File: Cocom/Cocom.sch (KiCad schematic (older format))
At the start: 19 parts

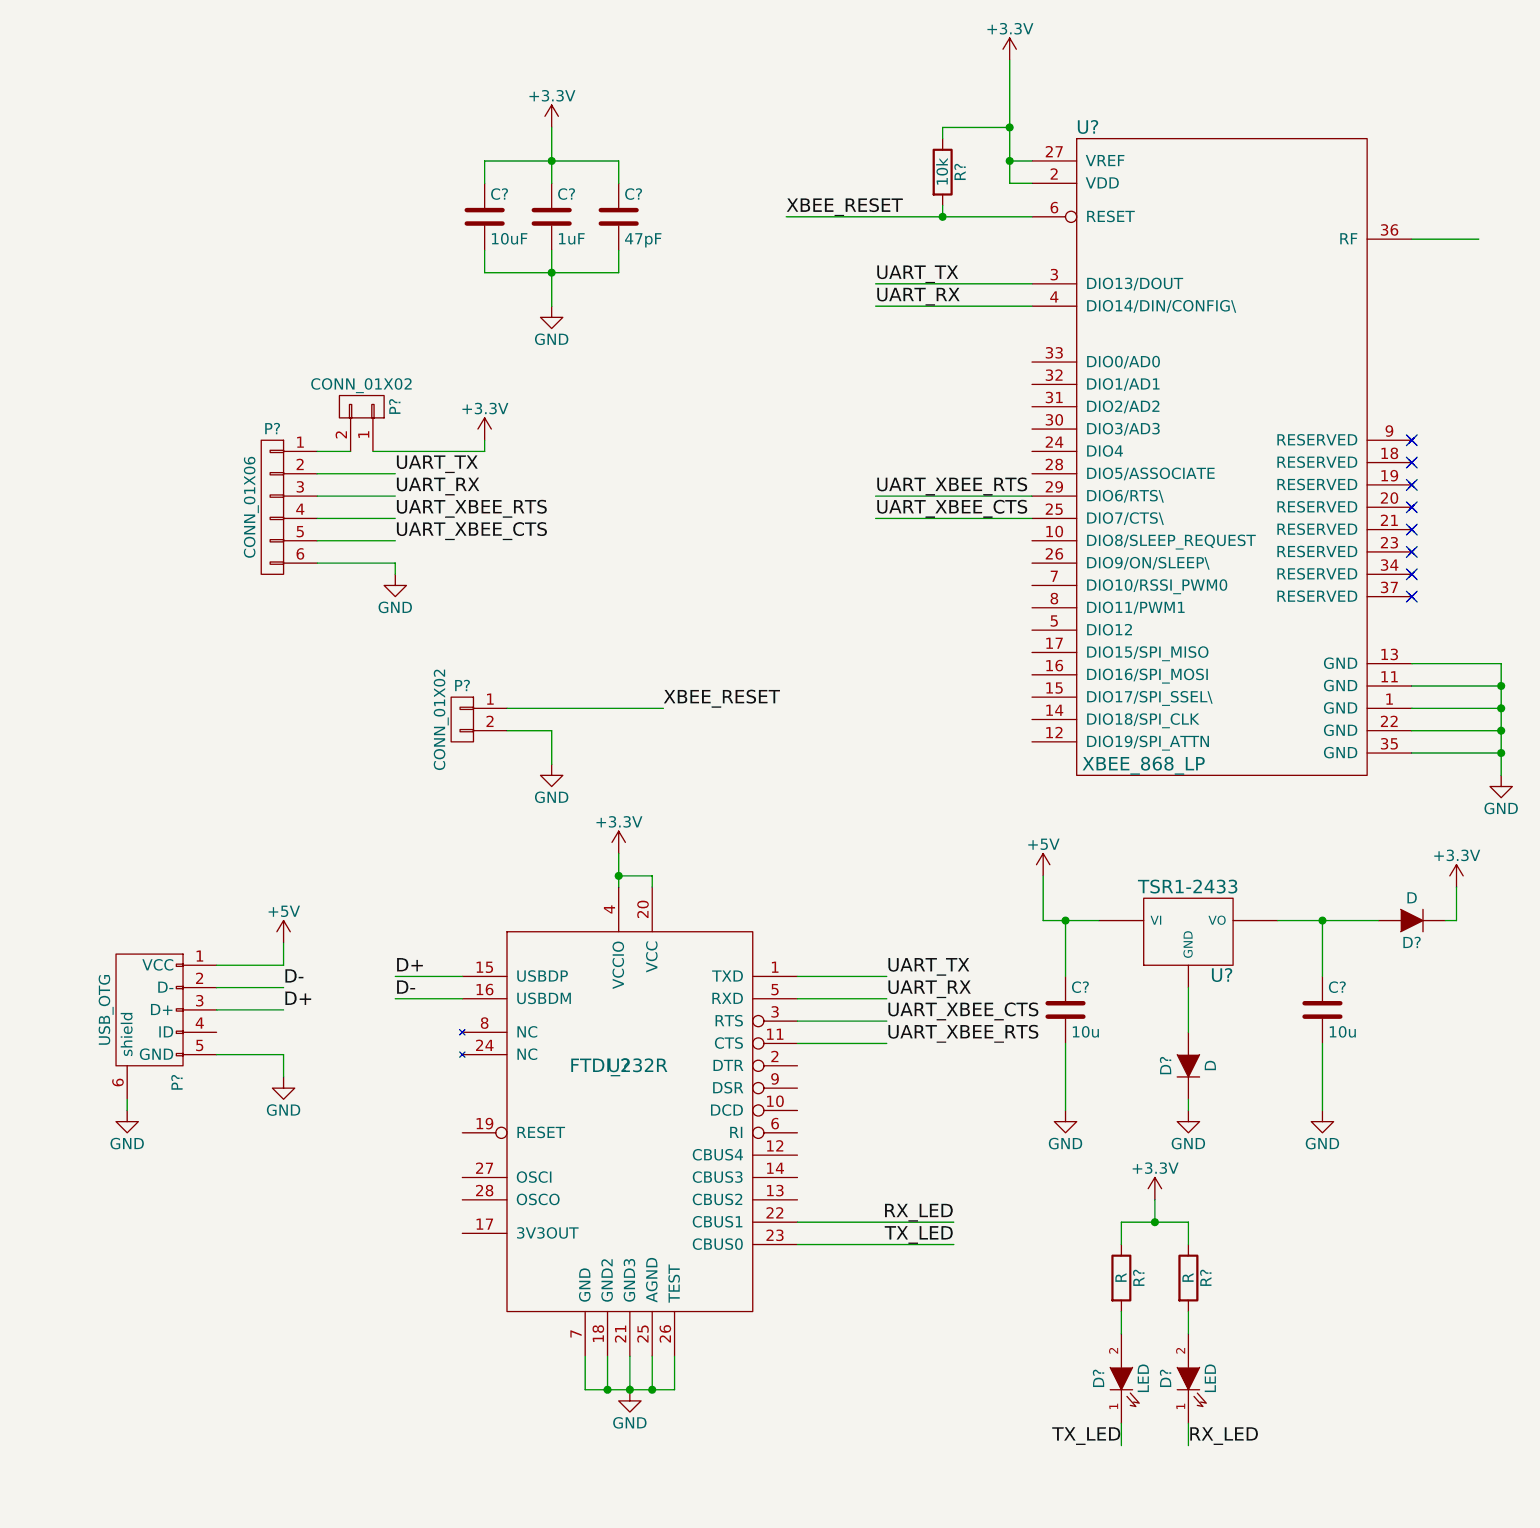
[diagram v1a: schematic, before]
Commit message: Add Cocom sch + pcb + some footprint
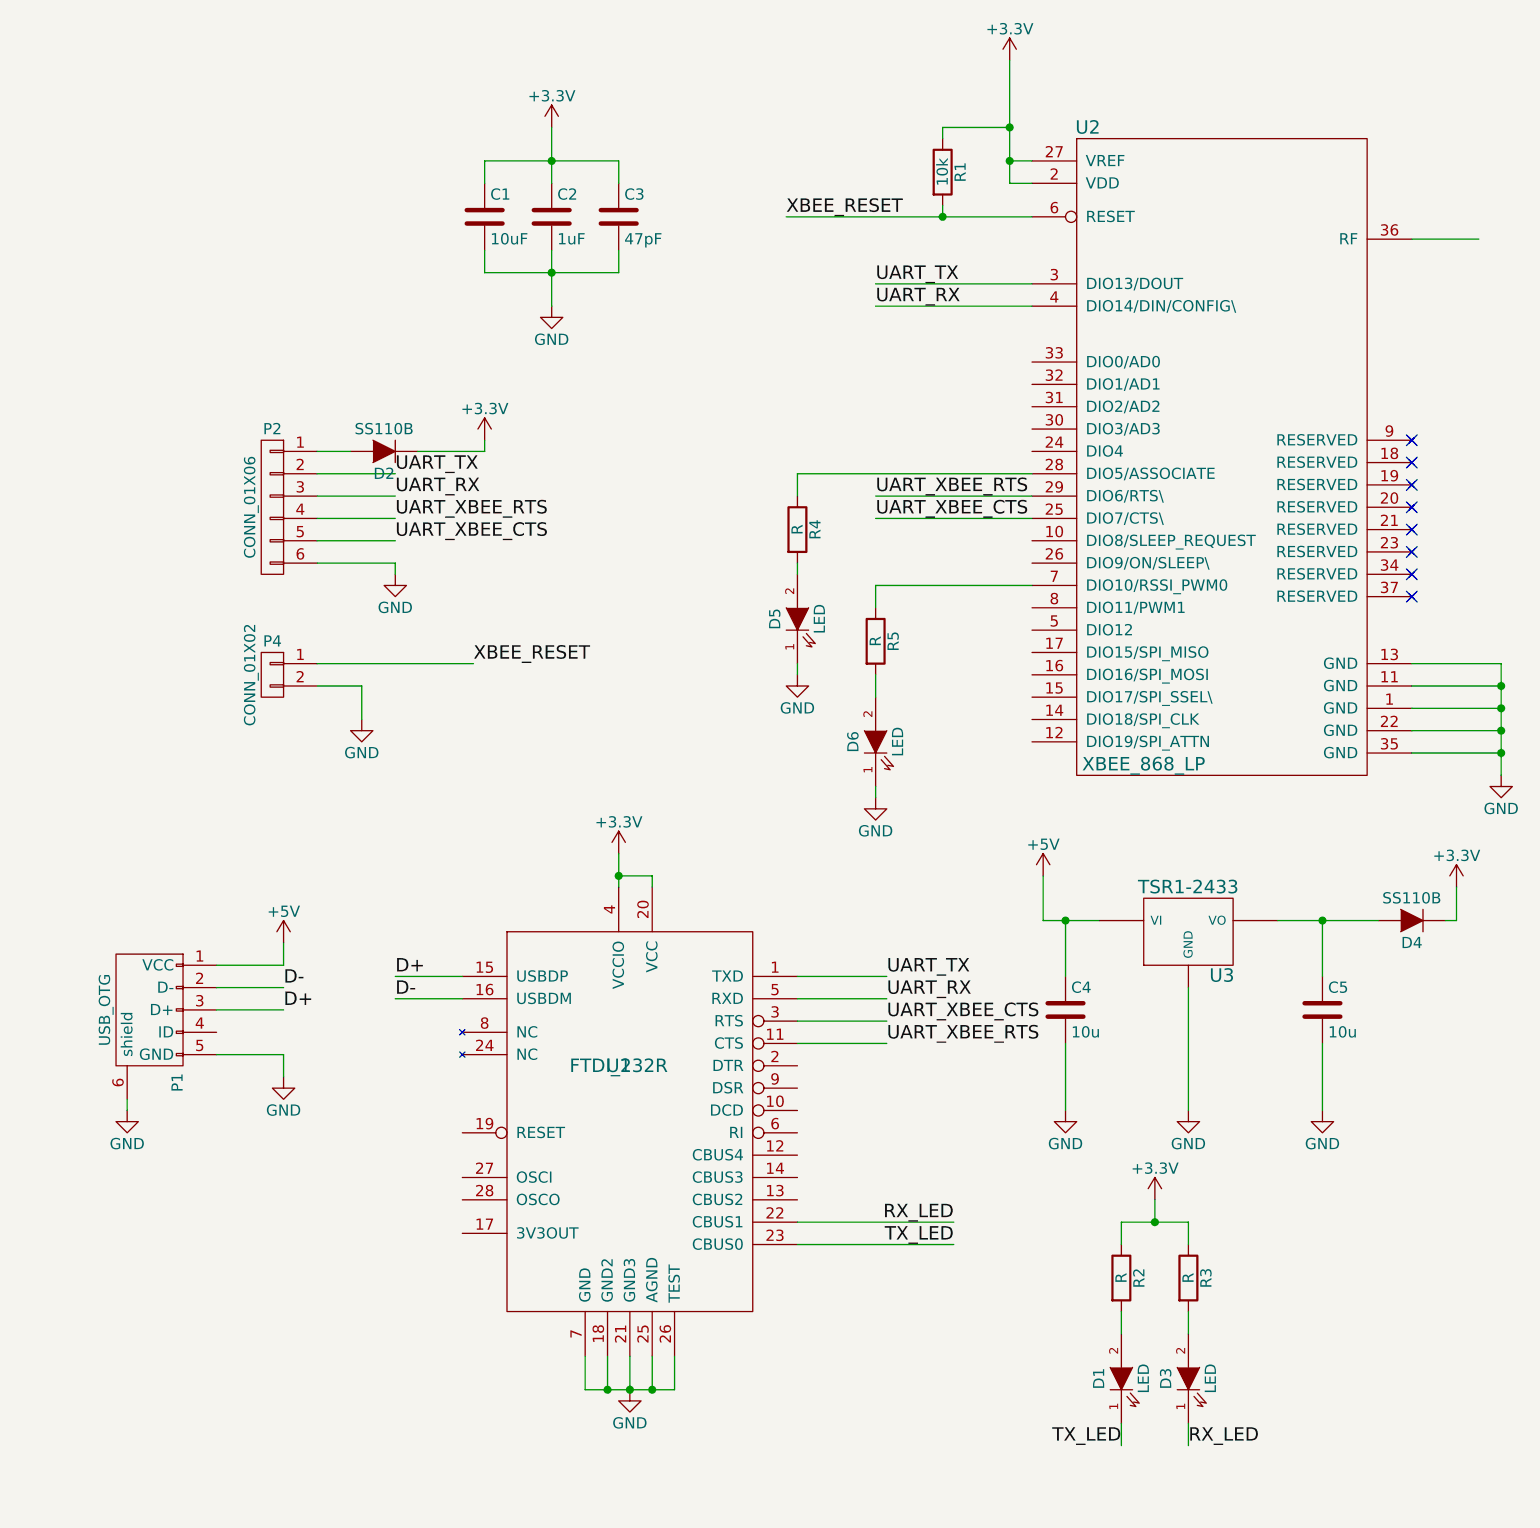
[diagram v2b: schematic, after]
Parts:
- removed D?: D, symbol D
- removed P?: CONN_01X02, symbol CONN_01X02
- added D2: SS110B, espitall:SOD5336X244, symbol D
- added D5, D6: LED, LEDs:LED_0603, symbol LED
- added R4, R5: R, Resistors_SMD:R_0603_HandSoldering, symbol R
- C1, C2, C3, C4, C5: renamed from C?; footprint (none) -> Capacitors_SMD:C_0603_HandSoldering
- D1, D3: renamed from D?; footprint (none) -> LEDs:LED_0603
- D4: renamed from D?; value D -> SS110B; footprint (none) -> espitall:SOD5336X244
- P1: renamed from P?; footprint (none) -> Connect:USB_Micro-B_10103594-0001LF
- P2: renamed from P?; footprint (none) -> espitall:BM06B-SRSS-TB(LFSN)
- P4: renamed from P?; footprint (none) -> Pin_Headers:Pin_Header_Straight_1x02
- R1, R2, R3: renamed from R?; footprint (none) -> Resistors_SMD:R_0603_HandSoldering
- U1: renamed from U?; footprint (none) -> Housings_SSOP:SSOP-28_5.3x10.2mm_Pitch0.65mm
- U2: renamed from U?; footprint (none) -> espitall:XBEE_868_LP
- U3: renamed from U?; footprint (none) -> espitall:TSR-1
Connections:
- net +3V3: now also D2.1 (K)
- net GND: now also U3.2 (GND), D5.1 (K), D6.1 (K)
- net at U2.28 (DIO5/ASSOCIATE): now also R4.1
- net at U2.7 (DIO10/RSSI_PWM0): now also R5.1
- net at P2.1 (P1): now also D2.2 (A)
- new net: D6.2 (A), R5.2
- new net: D5.2 (A), R4.2
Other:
- moved on the sheet: P4

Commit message: add module add footprint SPSGRF-868 for future com board
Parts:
- C1, C2, C3, C4, C5: symbol C -> device:C
- D1, D3, D5, D6: symbol LED -> Cocom-rescue:LED-RESCUE-Cocom
- D2, D4: symbol D -> device:D
- P1: symbol USB_OTG -> Cocom-rescue:USB_OTG-RESCUE-Cocom
- P2: symbol CONN_01X06 -> Cocom-rescue:CONN_01X06-RESCUE-Cocom
- P4: symbol CONN_01X02 -> Cocom-rescue:CONN_01X02-RESCUE-Cocom
- R1, R2, R3, R4, R5: symbol R -> device:R
- U1: symbol FTDI_232R -> espitall:FTDI_232R
- U2: symbol XBEE_868_LP -> espitall:XBEE_868_LP
- U3: symbol TSR1-2433 -> espitall:TSR1-2433
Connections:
- wire segments 88 -> 106
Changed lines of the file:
@@
-EESchema Schematic File Version 2
-LIBS:power
-LIBS:device
-LIBS:transistors
-LIBS:conn
-LIBS:linear
-LIBS:regul
-LIBS:74xx
-LIBS:cmos4000
-LIBS:adc-dac
-LIBS:memory
-LIBS:xilinx
-LIBS:microcontrollers
-LIBS:dsp
-LIBS:microchip
-LIBS:analog_switches
-LIBS:motorola
-LIBS:texas
-LIBS:intel
-LIBS:audio
-LIBS:interface
-LIBS:digital-audio
-LIBS:philips
-LIBS:display
-LIBS:cypress
-LIBS:siliconi
-LIBS:opto
-LIBS:atmel
-LIBS:contrib
-LIBS:valves
-LIBS:espitall
+EESchema Schematic File Version 4
 LIBS:Cocom-cache
-EELAYER 25 0
+EELAYER 26 0
 EELAYER END
 $Descr A4 11693 8268
@@
 $EndDescr
 $Comp
-L XBEE_868_LP U2
+L espitall:XBEE_868_LP U2
 U 1 1 575D6616
 P 5500 2900
@@
 $EndComp
 $Comp
-L R R1
+L device:R R1
 U 1 1 575D66C5
 P 4400 1850
@@
 $EndComp
 $Comp
-L GND #PWR01
+L power:GND #PWR01
 U 1 1 575D6769
 P 6900 4550
@@
 $EndComp
 $Comp
-L +3.3V #PWR02
+L power:+3.3V #PWR02
 U 1 1 575D67A9
 P 4700 1350
@@
 UART_RX
 $Comp
-L C C3
+L device:C C3
 U 1 1 575D6A69
 P 2950 2050
@@
 $EndComp
 $Comp
-L C C2
+L device:C C2
 U 1 1 575D6B1C
 P 2650 2050
@@
 $EndComp
 $Comp
-L C C1
+L device:C C1
 U 1 1 575D6B63
 P 2350 2050
@@
 $EndComp
 $Comp
-L GND #PWR03
+L power:GND #PWR03
 U 1 1 575D6CA6
 P 2650 2450
@@
 $EndComp
 $Comp
-L +3.3V #PWR04
+L power:+3.3V #PWR04
 U 1 1 575D6CC4
 P 2650 1650
@@
 UART_XBEE_CTS
 $Comp
-L +3.3V #PWR05
+L power:+3.3V #PWR05
 U 1 1 57651A1C
 P 2350 3050
@@
 $EndComp
 $Comp
-L GND #PWR06
+L power:GND #PWR06
 U 1 1 57651A3A
 P 1950 3650
@@
 $EndComp
 $Comp
-L CONN_01X06 P2
+L Cocom-rescue:CONN_01X06-RESCUE-Cocom P2
 U 1 1 57651AEE
 P 1400 3350
@@
 $EndComp
 $Comp
-L CONN_01X02 P4
+L Cocom-rescue:CONN_01X02-RESCUE-Cocom P4
 U 1 1 57651E65
 P 1400 4100
@@
 XBEE_RESET
 $Comp
-L GND #PWR07
+L power:GND #PWR07
 U 1 1 57652701
 P 1800 4300
@@
 XBEE_RESET
 $Comp
-L FTDI_232R U1
+L espitall:FTDI_232R U1
 U 1 1 5785DDA4
 P 2950 5850
@@
 UART_XBEE_CTS
 $Comp
-L TSR1-2433 U3
+L espitall:TSR1-2433 U3
 U 1 1 5785EA0C
 P 5500 5250
@@
 $EndComp
 $Comp
-L GND #PWR08
+L power:GND #PWR08
 U 1 1 5785EBDB
 P 5500 6050
@@
 $EndComp
 $Comp
-L +3.3V #PWR09
+L power:+3.3V #PWR09
 U 1 1 5785ECAB
 P 6700 5050
@@
 $EndComp
 $Comp
-L +5V #PWR010
+L power:+5V #PWR010
 U 1 1 5785F10F
 P 4850 5000
@@
 $EndComp
 $Comp
-L C C4
+L device:C C4
 U 1 1 5785F1FF
 P 4950 5600
@@
 $EndComp
 $Comp
-L C C5
+L device:C C5
 U 1 1 5785F2E7
 P 6100 5600
@@
 $EndComp
 $Comp
-L GND #PWR011
+L power:GND #PWR011
 U 1 1 5785F353
 P 6100 6050
@@
 $EndComp
 $Comp
-L GND #PWR012
+L power:GND #PWR012
 U 1 1 5785F39A
 P 4950 6050
@@
 $EndComp
 $Comp
-L +3.3V #PWR013
+L power:+3.3V #PWR013
 U 1 1 5785FA14
 P 2950 4900
@@
 $EndComp
 $Comp
-L GND #PWR014
+L power:GND #PWR014
 U 1 1 5785FC92
 P 3000 7300
@@
 $EndComp
 $Comp
-L USB_OTG P1
+L Cocom-rescue:USB_OTG-RESCUE-Cocom P1
 U 1 1 578600B2
 P 850 5600
@@
 $EndComp
 $Comp
-L GND #PWR015
+L power:GND #PWR015
 U 1 1 57860790
 P 750 6050
@@
 $EndComp
 $Comp
-L GND #PWR016
+L power:GND #PWR016
 U 1 1 578607C2
 P 1450 5900
@@
 $EndComp
 $Comp
-L +5V #PWR017
+L power:+5V #PWR017
 U 1 1 57860828
 P 1450 5300
@@
 D-
 $Comp
-L D D4
+L device:D D4
 U 1 1 57861004
 P 6500 5200
@@
 $EndComp
 $Comp
-L R R3
+L device:R R3
 U 1 1 578C75BB
 P 5500 6800
@@
 $EndComp
 $Comp
-L LED D3
+L Cocom-rescue:LED-RESCUE-Cocom D3
 U 1 1 578C762C
 P 5500 7250
@@
 $EndComp
 $Comp
-L R R2
+L device:R R2
 U 1 1 578C7A39
 P 5200 6800
@@
 $EndComp
 $Comp
-L LED D1
+L Cocom-rescue:LED-RESCUE-Cocom D1
 U 1 1 578C7A8F
 P 5200 7250
@@
 	4700 1900 4800 1900
 Wire Wire Line
-	4700 1350 4700 1900
+	4700 1350 4700 1650
 Connection ~ 4700 1800
 Connection ~ 4700 1650
 Wire Wire Line
-	6900 4050 6900 4550
+	6900 4050 6900 4150
 Wire Wire Line
 	6900 4050 6500 4050
@@
 	2950 1800 2950 1900
 Wire Wire Line
-	2350 1800 2950 1800
+	2350 1800 2650 1800
 Wire Wire Line
 	2350 1800 2350 1900
 Wire Wire Line
-	2650 1650 2650 1900
+	2650 1650 2650 1800
 Connection ~ 2650 1800
 Wire Wire Line
 	2350 2200 2350 2300
 Wire Wire Line
-	2350 2300 2950 2300
+	2350 2300 2650 2300
 Wire Wire Line
 	2950 2300 2950 2200
 Wire Wire Line
-	2650 2200 2650 2450
+	2650 2200 2650 2300
 Connection ~ 2650 2300
 Wire Wire Line
@@
 	4400 1650 4700 1650
 Wire Wire Line
-	3700 2050 4800 2050
+	3700 2050 4400 2050
 Wire Wire Line
 	4800 3300 4100 3300
@@
 	4150 5750 3750 5750
 Wire Wire Line
-	4850 5200 5100 5200
+	4850 5200 4950 5200
 Wire Wire Line
 	4850 5200 4850 5000
 Wire Wire Line
-	5900 5200 6350 5200
+	5900 5200 6100 5200
 Wire Wire Line
 	5500 5500 5500 6050
@@
 	6100 5750 6100 6050
 Wire Wire Line
-	2950 4900 2950 5050
+	2950 4900 2950 5000
 Wire Wire Line
 	3100 5050 3100 5000
@@
 	2800 7150 2800 7300
 Wire Wire Line
-	2800 7300 3200 7300
+	2800 7300 2900 7300
 Wire Wire Line
 	2900 7150 2900 7300
@@
 	5200 6650 5200 6550
 Wire Wire Line
-	5200 6550 5500 6550
+	5200 6550 5350 6550
 Wire Wire Line
 	5500 6550 5500 6650
@@
 	3750 6650 4450 6650
 $Comp
-L +3.3V #PWR018
+L power:+3.3V #PWR018
 U 1 1 578C8B6B
 P 5350 6450
@@
 $EndComp
 $Comp
-L D D2
+L device:D D2
 U 1 1 59352BEC
 P 1900 3100
@@
 	2050 3100 2350 3100
 $Comp
-L R R5
+L device:R R5
 U 1 1 593542E6
 P 4100 3950
@@
 $EndComp
 $Comp
-L LED D6
+L Cocom-rescue:LED-RESCUE-Cocom D6
 U 1 1 59354475
 P 4100 4400
@@
 $EndComp
 $Comp
-L GND #PWR019
+L power:GND #PWR019
 U 1 1 593546AF
 P 4100 4650
@@
 	4100 3700 4100 3800
 $Comp
-L R R4
+L device:R R4
 U 1 1 5935485B
 P 3750 3450
@@
 $EndComp
 $Comp
-L LED D5
+L Cocom-rescue:LED-RESCUE-Cocom D5
 U 1 1 593548C8
 P 3750 3850
@@
 $EndComp
 $Comp
-L GND #PWR020
+L power:GND #PWR020
 U 1 1 59354978
 P 3750 4100
@@
 Wire Wire Line
 	3750 3200 4800 3200
+Wire Wire Line
+	4700 1800 4700 1900
+Wire Wire Line
+	4700 1650 4700 1800
+Wire Wire Line
+	6900 4150 6900 4250
+Wire Wire Line
+	6900 4250 6900 4350
+Wire Wire Line
+	6900 4350 6900 4450
+Wire Wire Line
+	6900 4450 6900 4550
+Wire Wire Line
+	2650 1800 2950 1800
+Wire Wire Line
+	2650 1800 2650 1900
+Wire Wire Line
+	2650 2300 2950 2300
+Wire Wire Line
+	2650 2300 2650 2450
+Wire Wire Line
+	4400 2050 4800 2050
+Wire Wire Line
+	2950 5000 2950 5050
+Wire Wire Line
+	2900 7300 3000 7300
+Wire Wire Line
+	3000 7300 3100 7300
+Wire Wire Line
+	3100 7300 3200 7300
+Wire Wire Line
+	6100 5200 6350 5200
+Wire Wire Line
+	4950 5200 5100 5200
+Wire Wire Line
+	5350 6550 5500 6550
 $EndSCHEMATC
